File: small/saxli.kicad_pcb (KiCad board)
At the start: 4 copper layers, 160.5 x 102.4 mm, 176 parts, among them IC1 PIC32MX350F256H-V_PT, IC2 SIM808, J1 78800-0001, J10 Conn_01x06_Female, J11 Conn_Coaxial, J12 Conn_Coaxial, J2 Screw_Terminal_01x02, J3 Micro_SD_Card, J4 Conn_01x05_Female, J5 Conn_02x04_Odd_Even, J6 RJ45_Amphenol_RJMG1BD3B8K1ANR, J7 Screw_Terminal_01x08, J8 Screw_Terminal_01x08, J9 Screw_Terminal_01x08, Q1 2N7002, Q2 2N7002, Q3 2N7002, U1 LM358, U10 TPS5430DDAR, U11 EL357N(C)(TA)-G, U12 EL357N(C)(TA)-G, U13 ASSR-1218, U15 ASSR-1218, U16 SRV05-4, U18 ULN2003A, U2 LM7805_TO220, U20 TPS5430DDAR, U3 LD1117S33TR_SOT223, U4 ENC28J60x-SS, U5 AT25M02, U6 EL357N(C)(TA)-G, U7 EL357N(C)(TA)-G, U8 PCF8563T, U9 ISO1540, Y1 Crystal, Y2 Crystal

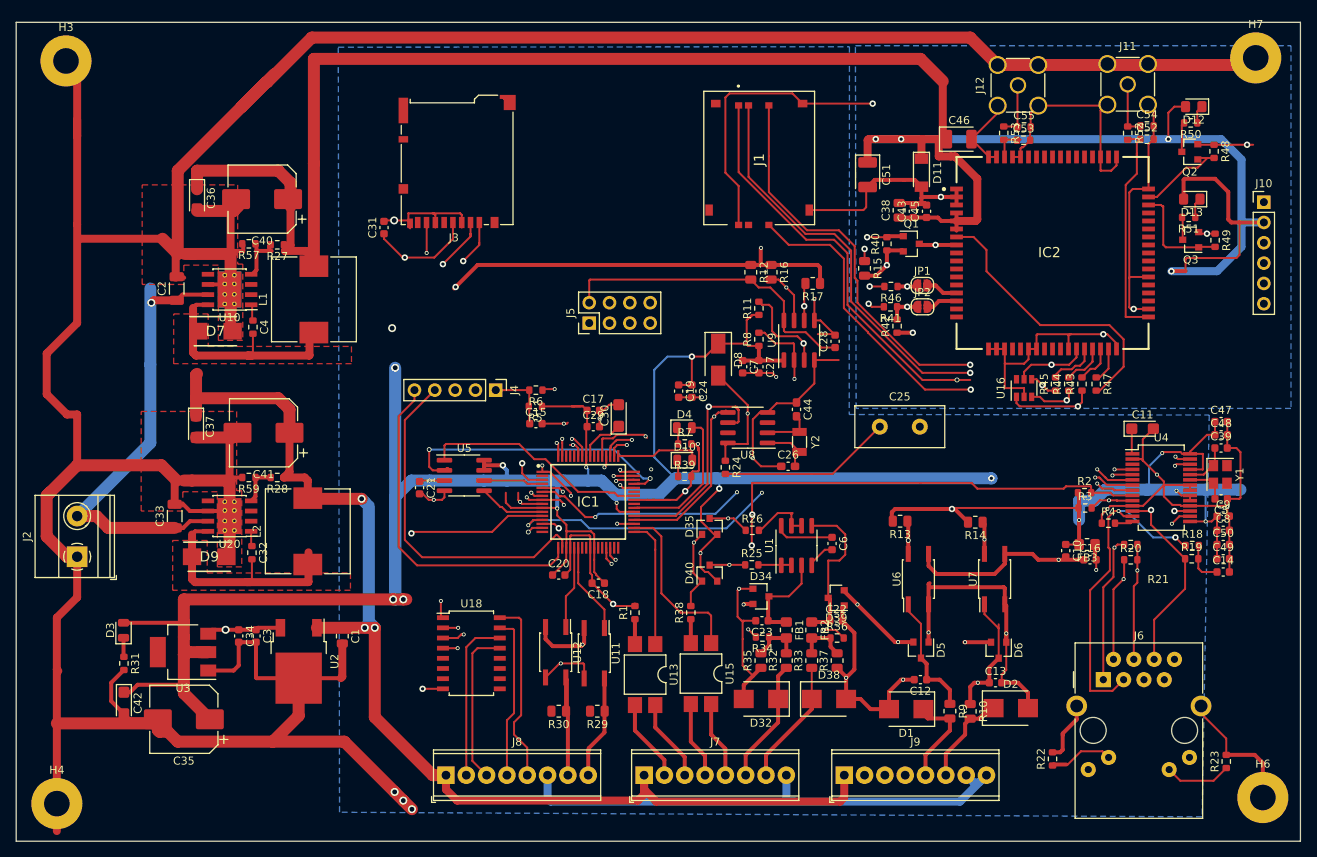
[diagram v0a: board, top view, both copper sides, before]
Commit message: connector rotated.
added rs485 output.

TODO: add bluetooth port.
check all parts
preaper bom list
prepare mouser list
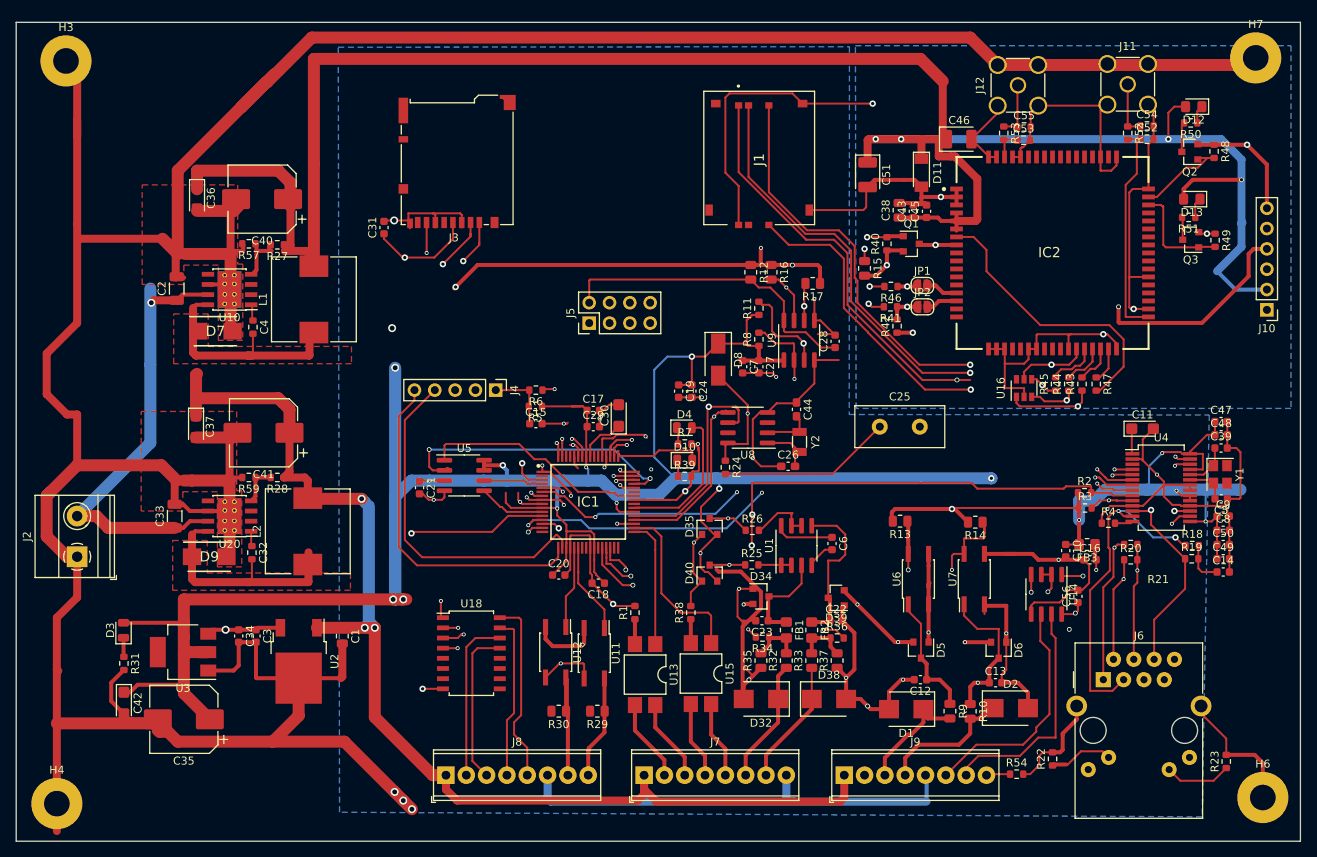
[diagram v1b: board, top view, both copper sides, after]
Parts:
- added C56: 0.1u, Capacitor_SMD:C_0603_1608Metric, F.Cu at (170.8, 92.6)
- added R54: 10k, Resistor_SMD:R_0603_1608Metric, F.Cu at (163.2, 114.8)
- added U14: ST485EBDR, Package_SO:SOIC-8_3.9x4.9mm_P1.27mm, F.Cu at (166.9, 92.3)
- moved J10 13.5 mm to (194.4, 56.8), turned to 180 degrees
- moved U7 2.54 mm to (157.9, 90.4)
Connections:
- IC1 pad 28: Net-(IC1-Pad28) -> 485_DE
- J7 pad 8: GNDPWR -> GND
- J8 pad 6: GNDPWR -> GND
- J9 pad 3: Net-(J9-Pad3) -> IS_IN0
- J9 pad 4: Net-(J9-Pad4) -> IS_IN1
- J9 pad 5: IS_IN0 -> GND
- J9 pad 6: IS_IN1 -> 485_A
- J9 pad 7: GNDPWR -> 485_B
- J9 pad 8: GNDPWR -> Net-(J9-Pad8)
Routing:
- net GND: track 1047.8 -> 1163.0 mm, vias 36 -> 38
- net U1TX485: track 57.9 -> 160.6 mm, vias 1 -> 3
- net U1RX485: track 55.4 -> 153.0 mm, vias 1 -> 2
- net VDD5: track 149.8 -> 217.2 mm, vias 3 -> 5
- net GNDPWR: track 65.5 -> 0.00 mm
- net 485_DE: track 0.00 -> 63.2 mm, vias 0 -> 2
- net 485_A: track 0.00 -> 29.4 mm
- net 485_B: track 0.00 -> 29.3 mm
- net POWER_SIM: track 292.0 -> 268.9 mm
- net /sim868/SIM_RX: track 51.0 -> 57.4 mm, vias 1 -> 2
- net IS_IN1: track 12.0 -> 17.1 mm
- net /sim868/SIM_TX: track 47.2 -> 51.0 mm
- net MCU_0: track 43.6 -> 46.9 mm
- net Net-(J9-Pad8): track 0.00 -> 3.00 mm
- net IS_IN0: track 12.5 -> 14.6 mm
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- added copper zone on F.Cu, net Net-(C4-Pad2)
- removed copper zone on F.Cu, net (none)
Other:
- board text added: "SoftMaster LTD 2020"

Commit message: GPS connector moved,
antenna matching networks removed

SUPERCAPACITOR from jlpcb used.
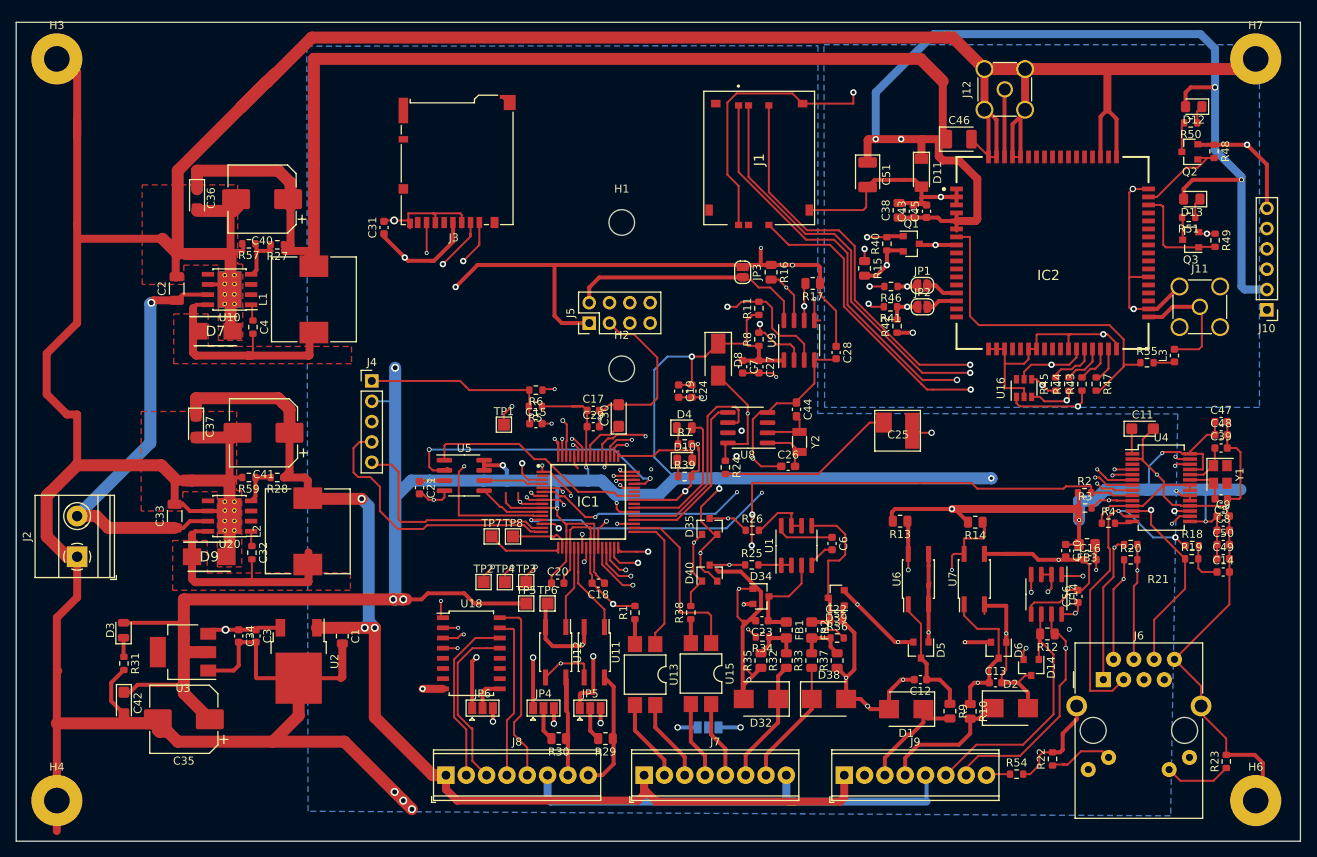
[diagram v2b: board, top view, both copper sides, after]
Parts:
- removed C52, C53, C54, C55: NA, Resistor_SMD:R_0603_1608Metric
- removed R52, R53: R, Resistor_SMD:R_0603_1608Metric
- added D14: PSM712-LF-T7, Package_TO_SOT_SMD:SOT-23, F.Cu at (165.0, 101.5)
- added H1: MountingHole, MountingHole:MountingHole_3.2mm_M3, F.Cu at (113.8, 45.8)
- added H2: MountingHole, MountingHole:MountingHole_3.2mm_M3, F.Cu at (113.8, 64.1)
- added JP3: Jumper, Jumper:SolderJumper-2_P1.3mm_Open_RoundedPad1.0x1.5mm, F.Cu at (128.9, 52.1)
- added JP4: Jumper_NC_Dual, Jumper:SolderJumper-3_P1.3mm_Open_Pad1.0x1.5mm, F.Cu at (104.0, 106.6)
- added JP5: Jumper_NC_Dual, Jumper:SolderJumper-3_P1.3mm_Open_Pad1.0x1.5mm, F.Cu at (109.9, 106.6)
- added JP6: Jumper_NC_Dual, Jumper:SolderJumper-3_P1.3mm_Open_Pad1.0x1.5mm, F.Cu at (96.4, 106.6)
- added JP7: Jumper_NC_Dual, Jumper:SolderJumper-3_P1.3mm_Open_Pad1.0x1.5mm, B.Cu at (124.6, 109.0)
- added L3: INDUCTOR, Inductor_SMD:L_0603_1608Metric, F.Cu at (182.9, 62.5)
- added R55: R, Resistor_SMD:R_0603_1608Metric, F.Cu at (179.5, 63.4)
- added TP1: TestPoint, TestPoint:TestPoint_Pad_1.5x1.5mm, F.Cu at (99.1, 71.1)
- added TP2: TestPoint, TestPoint:TestPoint_Pad_1.5x1.5mm, F.Cu at (96.5, 90.8)
- added TP3: TestPoint, TestPoint:TestPoint_Pad_1.5x1.5mm, F.Cu at (101.9, 90.8)
- added TP4: TestPoint, TestPoint:TestPoint_Pad_1.5x1.5mm, F.Cu at (99.2, 90.8)
- added TP5: TestPoint, TestPoint:TestPoint_Pad_1.5x1.5mm, F.Cu at (101.9, 93.5)
- added TP6: TestPoint, TestPoint:TestPoint_Pad_1.5x1.5mm, F.Cu at (104.5, 93.5)
- added TP7: TestPoint, TestPoint:TestPoint_Pad_1.5x1.5mm, F.Cu at (97.5, 85.1)
- added TP8: TestPoint, TestPoint:TestPoint_Pad_1.5x1.5mm, F.Cu at (100.2, 85.1)
- C25: footprint Capacitor_THT:C_Disc_D11.0mm_W5.0mm_P5.00mm -> small:XH414HG-IV01E
- R12: value R -> 120
- R41, R46: value 680 -> 1k
- moved R12 58.5 mm to (167.0, 97.3), turned to 180 degrees
- moved J11 29.2 mm to (186.1, 56.4)
- moved J4 15.5 mm to (82.5, 65.7), turned to 0 degrees
- moved R29 3.58 mm to (111.8, 110.4)
- moved R30 3.43 mm to (105.9, 110.4)
- moved C25 2.34 mm to (148.3, 71.9)
- moved J12 1.73 mm to (161.7, 29.2)
- moved C28 1.40 mm to (140.6, 62.1), turned to 270 degrees
- moved H3 1.17 mm to (43.2, 25.4)
- moved C20 1.02 mm to (105.8, 90.9)
- moved H6 0.97 mm to (193.0, 118.1)
- moved H4 0.38 mm to (43.2, 118.1)
- moved H7 0.13 mm to (193.0, 25.4)
- moved U11 0.13 mm to (110.4, 99.6)
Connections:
- C28 pad 1: /communication/VDD_ISO -> VDD5
- C28 pad 2: /communication/GND_ISO -> GND
- IC1 pad 15: GND -> /MCU/PGEC
- IC1 pad 16: Net-(IC1-Pad16) -> /MCU/PGED
- IC1 pad 17: /MCU/PGEC -> Net-(IC1-Pad17)
- IC1 pad 18: /MCU/PGED -> Net-(IC1-Pad18)
- IC1 pad 63: ADC_1 -> ADC_0
- IC1 pad 64: ADC_0 -> ADC_1
- J11 pad 1: Net-(C54-Pad1) -> GPS_ANT
- J12 pad 1: Net-(C55-Pad1) -> GSM_ANT
- J5 pad 1: /communication/VDD_ISO -> VDD5
- J5 pad 3: /communication/SDA_ISO -> GND
- J5 pad 5: /communication/SCL_ISO -> U2RX
- J5 pad 7: /communication/GND_ISO -> U2TX
- R11 pad 2: SCL1 -> SCL2
- R12 pad 1: VDD5 -> 485_B
- R12 pad 2: /communication/VDD_ISO -> 485_A
- R8 pad 2: SDA1 -> SDA2
- U9 pad 2: SDA1 -> SDA2
- U9 pad 3: SCL1 -> SCL2
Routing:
- net VDD5: track 217.2 -> 332.5 mm, vias 5 -> 9
- net SCL2: track 0.00 -> 57.2 mm, vias 0 -> 2
- net SDA2: track 0.00 -> 55.4 mm, vias 0 -> 2
- net 12V: track 171.8 -> 218.0 mm, vias 3 -> 7
- net SCL1: track 56.4 -> 27.3 mm, vias 2 -> 0
- net GND: track 1163.0 -> 1188.5 mm, vias 38 -> 39
- net ADC_1: track 34.3 -> 57.9 mm, vias 2 -> 3
- net SDA1: track 44.1 -> 22.1 mm, vias 2 -> 0
- net ADC_0: track 36.1 -> 56.9 mm, vias 2 -> 3
- net Net-(IC1-Pad27): track 0.00 -> 20.2 mm, vias 0 -> 2
- net U2RX: track 2.72 -> 22.8 mm
- net U2TX: track 4.25 -> 21.8 mm
- net Net-(IC1-Pad23): track 0.00 -> 16.9 mm, vias 0 -> 2
- net /sim868/SIM_TX: track 51.0 -> 67.7 mm
- net /sim868/SIM_RX: track 57.4 -> 73.8 mm, vias 2 -> 1
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
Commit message: minor updates
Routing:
- net GND: track 1188.5 -> 1197.9 mm
- net GSM_ANT: track 8.57 -> 15.8 mm
- net VDD3: track 468.7 -> 464.4 mm
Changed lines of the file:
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@@
     (thickness 1.6)
     (drawings 7)
-    (tracks 2291)
+    (tracks 2294)
     (zones 0)
     (modules 191)
@@
   )
   (setup
-    (last_trace_width 0.5)
+    (last_trace_width 1.5)
     (user_trace_width 0.5)
     (user_trace_width 1)
@@
   (segment (start 106.75 89.859) (end 106.693 89.916) (width 0.25) (layer F.Cu) (net 1))
   (segment (start 107.351 89.258) (end 106.75 89.859) (width 0.25) (layer F.Cu) (net 1))
-  (segment (start 160.64 33.005) (end 159.385 31.75) (width 0.5) (layer F.Cu) (net 1))
-  (segment (start 160.64 37.657) (end 160.64 33.005) (width 0.5) (layer F.Cu) (net 1))
-  (segment (start 162.64 33.575) (end 164.465 31.75) (width 0.5) (layer F.Cu) (net 1))
-  (segment (start 162.64 37.657) (end 162.64 33.575) (width 0.5) (layer F.Cu) (net 1))
   (segment (start 163.64 32.575) (end 164.465 31.75) (width 0.5) (layer F.Cu) (net 1))
   (segment (start 163.64 37.657) (end 163.64 32.575) (width 0.5) (layer F.Cu) (net 1))
@@
   (segment (start 180.706 56.657) (end 183.515 53.848) (width 0.5) (layer F.Cu) (net 1))
   (segment (start 179.64 56.657) (end 180.706 56.657) (width 0.5) (layer F.Cu) (net 1))
-  (segment (start 183.515 58.928) (end 177.927 58.928) (width 0.5) (layer In1.Cu) (net 1))
-  (segment (start 177.785 58.786) (end 177.785 56.657) (width 0.5) (layer In1.Cu) (net 1))
-  (segment (start 177.927 58.928) (end 177.785 58.786) (width 0.5) (layer In1.Cu) (net 1))
   (segment (start 174.498 31.75) (end 174.498 26.67) (width 1) (layer F.Cu) (net 1))
   (segment (start 173.64 32.608) (end 174.498 31.75) (width 0.5) (layer F.Cu) (net 1))
@@
   (segment (start 142.748 30.988) (end 142.748 29.591) (width 0.25) (layer F.Cu) (net 1))
   (segment (start 136.398 30.988) (end 142.748 30.988) (width 0.25) (layer F.Cu) (net 1))
+  (segment (start 159.64 32.259) (end 159.131 31.75) (width 1) (layer F.Cu) (net 1))
+  (segment (start 159.64 37.657) (end 159.64 32.259) (width 1) (layer F.Cu) (net 1))
+  (segment (start 163.64 32.321) (end 164.211 31.75) (width 1) (layer F.Cu) (net 1))
+  (segment (start 163.64 37.657) (end 163.64 32.321) (width 1) (layer F.Cu) (net 1))
+  (segment (start 177.785 56.657) (end 177.785 58.913) (width 1) (layer F.Cu) (net 1))
+  (segment (start 183.5 58.913) (end 183.515 58.928) (width 1) (layer F.Cu) (net 1))
+  (segment (start 177.785 58.913) (end 183.5 58.913) (width 1) (layer F.Cu) (net 1))
+  (segment (start 183.515 53.848) (end 188.595 53.848) (width 1) (layer F.Cu) (net 1))
+  (segment (start 188.595 53.848) (end 188.595 58.928) (width 1) (layer F.Cu) (net 1))
   (segment (start 57.912 84.025) (end 58.977 84.025) (width 0.5) (layer F.Cu) (net 2))
   (segment (start 58.977 84.025) (end 59.817 83.185) (width 0.5) (layer F.Cu) (net 2))
@@
   (segment (start 172.861002 80.629) (end 174.242002 79.248) (width 1.5) (layer B.Cu) (net 21))
   (segment (start 170.958 80.629) (end 172.861002 80.629) (width 1.5) (layer B.Cu) (net 21))
-  (segment (start 190.881 79.248) (end 191.135 79.248) (width 1.5) (layer B.Cu) (net 21))
   (segment (start 85.471 92.964) (end 85.471 80.137) (width 1.5) (layer B.Cu) (net 21))
   (segment (start 113.025499 79.876501) (end 118.435497 79.876501) (width 1.5) (layer B.Cu) (net 21))
@@
   (segment (start 186.783 79.282) (end 186.817 79.248) (width 0.25) (layer B.Cu) (net 21))
   (segment (start 186.783 83.219) (end 186.783 79.282) (width 0.25) (layer B.Cu) (net 21))
-  (segment (start 186.817 79.248) (end 190.881 79.248) (width 1.5) (layer B.Cu) (net 21))
   (segment (start 184.829 74.769) (end 186.402 74.769) (width 0.25) (layer F.Cu) (net 21))
   (segment (start 186.402 74.769) (end 186.436 74.803) (width 0.25) (layer F.Cu) (net 21))
@@
   (segment (start 149.479 53.848) (end 150.368 53.848) (width 0.5) (layer In1.Cu) (net 186))
   (segment (start 161.64 29.495) (end 161.925 29.21) (width 0.5) (layer F.Cu) (net 187))
-  (segment (start 161.64 37.657) (end 161.64 29.495) (width 0.5) (layer F.Cu) (net 187))
+  (segment (start 161.64 37.657) (end 161.64 36.48) (width 0.5) (layer F.Cu) (net 187))
+  (segment (start 161.64 36.48) (end 161.64 29.495) (width 0.5) (layer F.Cu) (net 187))
+  (segment (start 161.671 29.972) (end 161.64 30.003) (width 1.5) (layer F.Cu) (net 187))
+  (segment (start 161.671 29.21) (end 161.671 29.972) (width 1.5) (layer F.Cu) (net 187))
+  (segment (start 161.64 36.48) (end 161.64 30.003) (width 1) (layer F.Cu) (net 187))
   (segment (start 185.737 31.95) (end 186.318 31.369) (width 0.25) (layer F.Cu) (net 188))
   (segment (start 185.737 33.401) (end 185.737 31.95) (width 0.25) (layer F.Cu) (net 188))
@@
   (segment (start 186.309 56.642) (end 186.055 56.388) (width 0.25) (layer F.Cu) (net 199))
   (segment (start 186.309 61.341) (end 186.309 56.642) (width 0.25) (layer F.Cu) (net 199))
-  (segment (start 179.64 57.657) (end 181.23 57.657) (width 0.5) (layer F.Cu) (net 199))
-  (segment (start 181.357 57.657) (end 182.626 56.388) (width 0.5) (layer F.Cu) (net 199))
-  (segment (start 181.23 57.657) (end 181.357 57.657) (width 0.5) (layer F.Cu) (net 199))
-  (segment (start 182.626 56.388) (end 186.055 56.388) (width 0.5) (layer F.Cu) (net 199))
+  (segment (start 181.865 57.657) (end 183.134 56.388) (width 1) (layer F.Cu) (net 199))
+  (segment (start 179.64 57.657) (end 181.865 57.657) (width 1) (layer F.Cu) (net 199))
+  (segment (start 183.134 56.388) (end 186.055 56.388) (width 1) (layer F.Cu) (net 199))
   (segment (start 100.203 85.09) (end 100.397 85.284) (width 0.25) (layer F.Cu) (net 206))
   (segment (start 111.351 88.61941) (end 113.91759 91.186) (width 0.25) (layer F.Cu) (net 200))

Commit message: BOM updated
Layout changed
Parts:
- C26, C44: value 15pf -> 20pf
- moved H2 17.3 mm to (96.8, 61.1)
- moved C30 2.58 mm to (114.2, 67.5)
- moved C17 2.32 mm to (110.6, 67.1)
- moved C29 2.32 mm to (110.6, 69.1)
- moved R6 1.65 mm to (103.0, 65.2)
- moved C15 1.65 mm to (103.0, 69.3)
- moved R5 1.65 mm to (103.0, 67.2)
- moved C18 1.36 mm to (111.8, 91.9), turned to 270 degrees
- moved C20 1.09 mm to (104.8, 91.3)
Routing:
- net VDD3: track 464.4 -> 548.7 mm, vias 18 -> 17
- net ADC_1: track 57.9 -> 46.1 mm
- net ADC_0: track 56.9 -> 45.2 mm
- net GND: track 1197.9 -> 1186.3 mm, vias 39 -> 43
- net POWER_SIM: track 285.0 -> 281.7 mm
- net Net-(C30-Pad1): track 5.90 -> 8.70 mm
- net MCU_1: track 58.8 -> 56.7 mm
- net Net-(IC1-Pad7): track 17.4 -> 18.9 mm

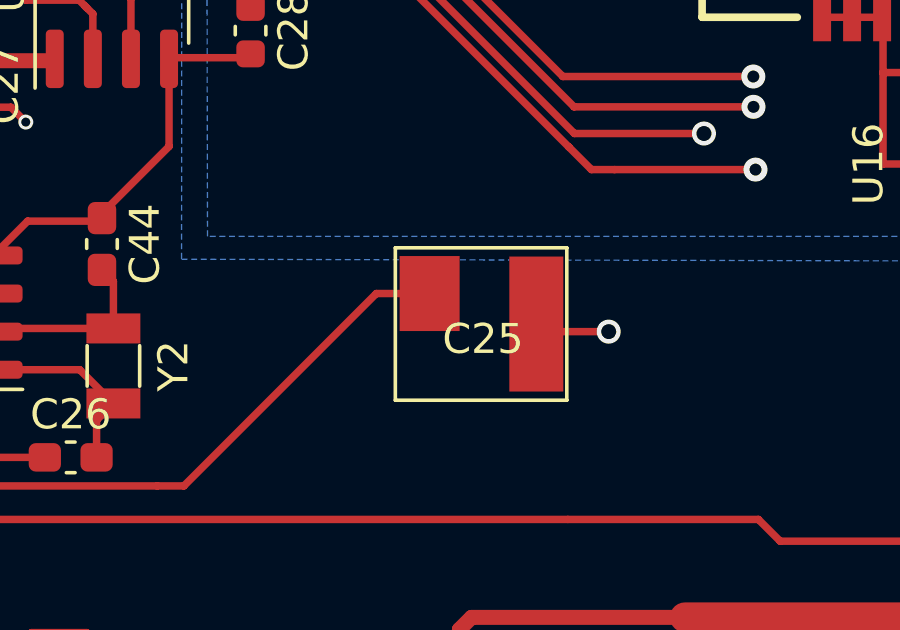
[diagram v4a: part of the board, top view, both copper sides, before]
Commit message: Battery Footprint changed.
Few mods
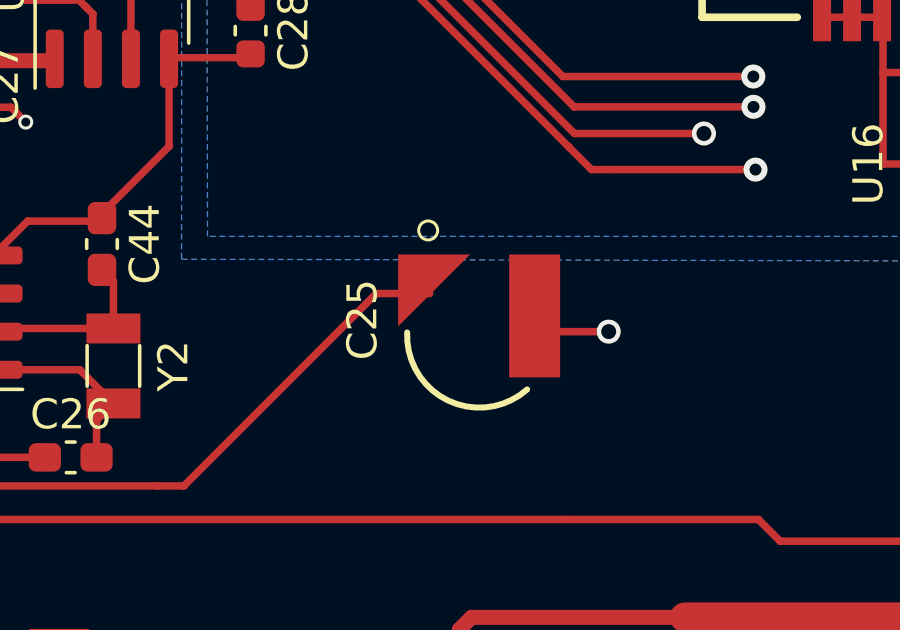
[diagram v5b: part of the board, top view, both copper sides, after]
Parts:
- C25: value SUPERCAP -> XH414HG-IV01E; footprint small:XH414HG-IV01E -> small:CAP_XH414HG-IV01E
- moved C25 0.40 mm to (148.2, 72.3), turned to 90 degrees
